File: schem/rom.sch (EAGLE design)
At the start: 27 parts, among them IC10 74HC32N, IC11 74HC32N, IC12 74HC32N, IC13 74HC32N, IC14 74HC04N, IC6 74HC374N, IC7 74HC08N, IC8 74HC377N, IC9 74HC377N

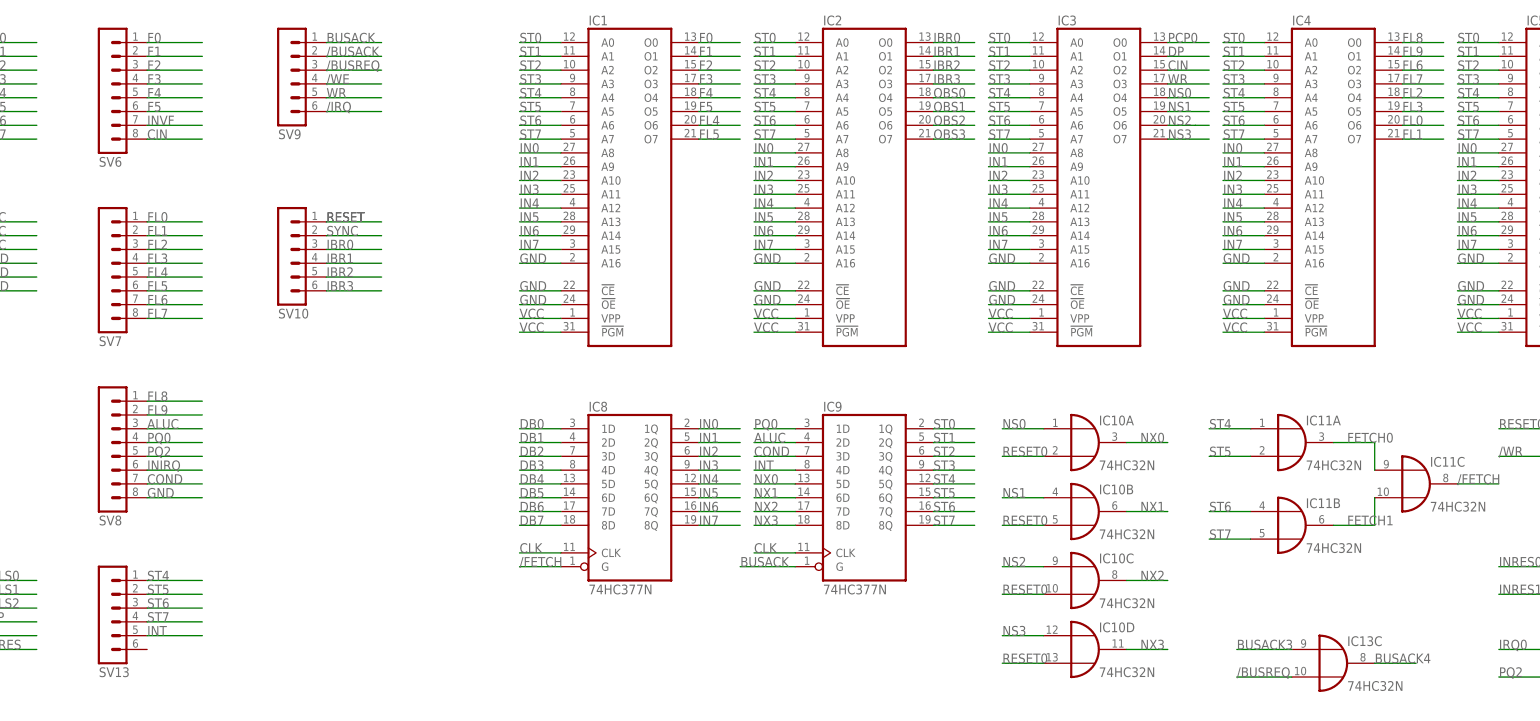
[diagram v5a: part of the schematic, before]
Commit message: swapped rom bits
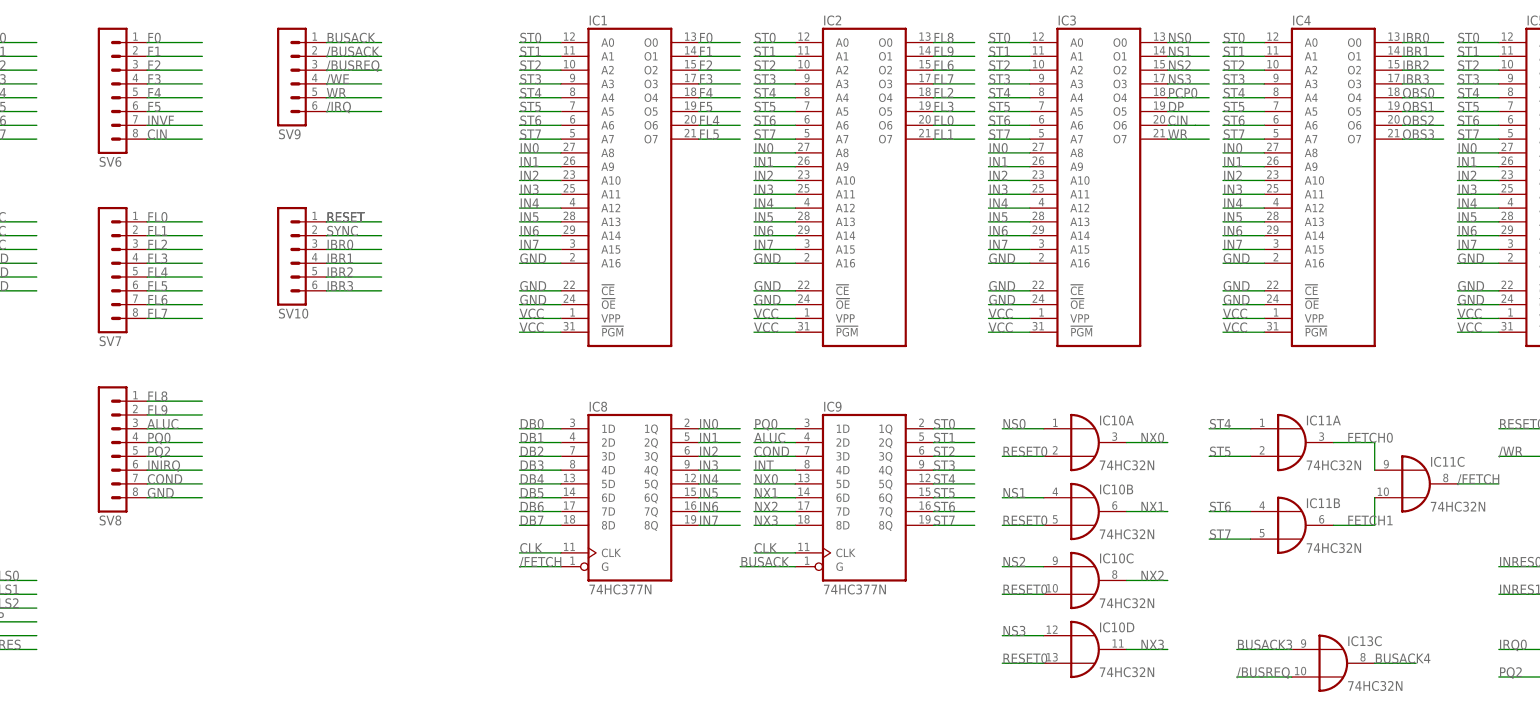
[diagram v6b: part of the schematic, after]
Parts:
- removed SV13: (no value), con-lstb:MA06-1
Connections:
- net CIN: now also IC3A.O6; no longer IC3A.O2
- net DP: now also IC3A.O5; no longer IC3A.O1
- net FL0: now also IC2A.O6; no longer IC4A.O6
- net FL1: now also IC2A.O7; no longer IC4A.O7
- net FL2: now also IC2A.O4; no longer IC4A.O4
- net FL3: now also IC2A.O5; no longer IC4A.O5
- net FL6: now also IC2A.O2; no longer IC4A.O2
- net FL7: now also IC2A.O3; no longer IC4A.O3
- net FL8: now also IC2A.O0; no longer IC4A.O0
- net FL9: now also IC2A.O1; no longer IC4A.O1
- net IBR0: now also IC4A.O0; no longer IC2A.O0
- net IBR1: now also IC4A.O1; no longer IC2A.O1
- net IBR2: now also IC4A.O2; no longer IC2A.O2
- net IBR3: now also IC4A.O3; no longer IC2A.O3
- net INT: no longer SV13.5
- net NS0: now also IC3A.O0; no longer IC3A.O4
- net NS1: now also IC3A.O1; no longer IC3A.O5
- net NS2: now also IC3A.O2; no longer IC3A.O6
- net NS3: now also IC3A.O3; no longer IC3A.O7
- net OBS0: now also IC4A.O4; no longer IC2A.O4
- net OBS1: now also IC4A.O5; no longer IC2A.O5
- net OBS2: now also IC4A.O6; no longer IC2A.O6
- net OBS3: now also IC4A.O7; no longer IC2A.O7
- net PCP0: now also IC3A.O4; no longer IC3A.O0
- net ST4: no longer SV13.1
- net ST5: no longer SV13.2
- net ST6: no longer SV13.3
- net ST7: no longer SV13.4
- net WR: now also IC3A.O7; no longer IC3A.O3
